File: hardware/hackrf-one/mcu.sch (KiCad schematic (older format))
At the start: 107 parts, among them J1 GSG-USB-MICRO-B, P1 1V8, P17 SSP0, P20 GPIO, P22 I2S, P23 DBGEN, P24 TRST, P25 LPC_ISP, P26 LPC_JTAG, P28 SD, P29 CPLD_JTAG, P3 GND, P30 BANK2_AUX, P8 VCC, SW1 DFU, SW2 RESET, U20 W25Q80BV, U21 TPS62410, U22 GSG-IP4220CZ6, U23 LPC4320FBD144, U24 GSG-XC2C64A-7VQG100C, X2 MCU_XTAL, X3 RTC_XTAL

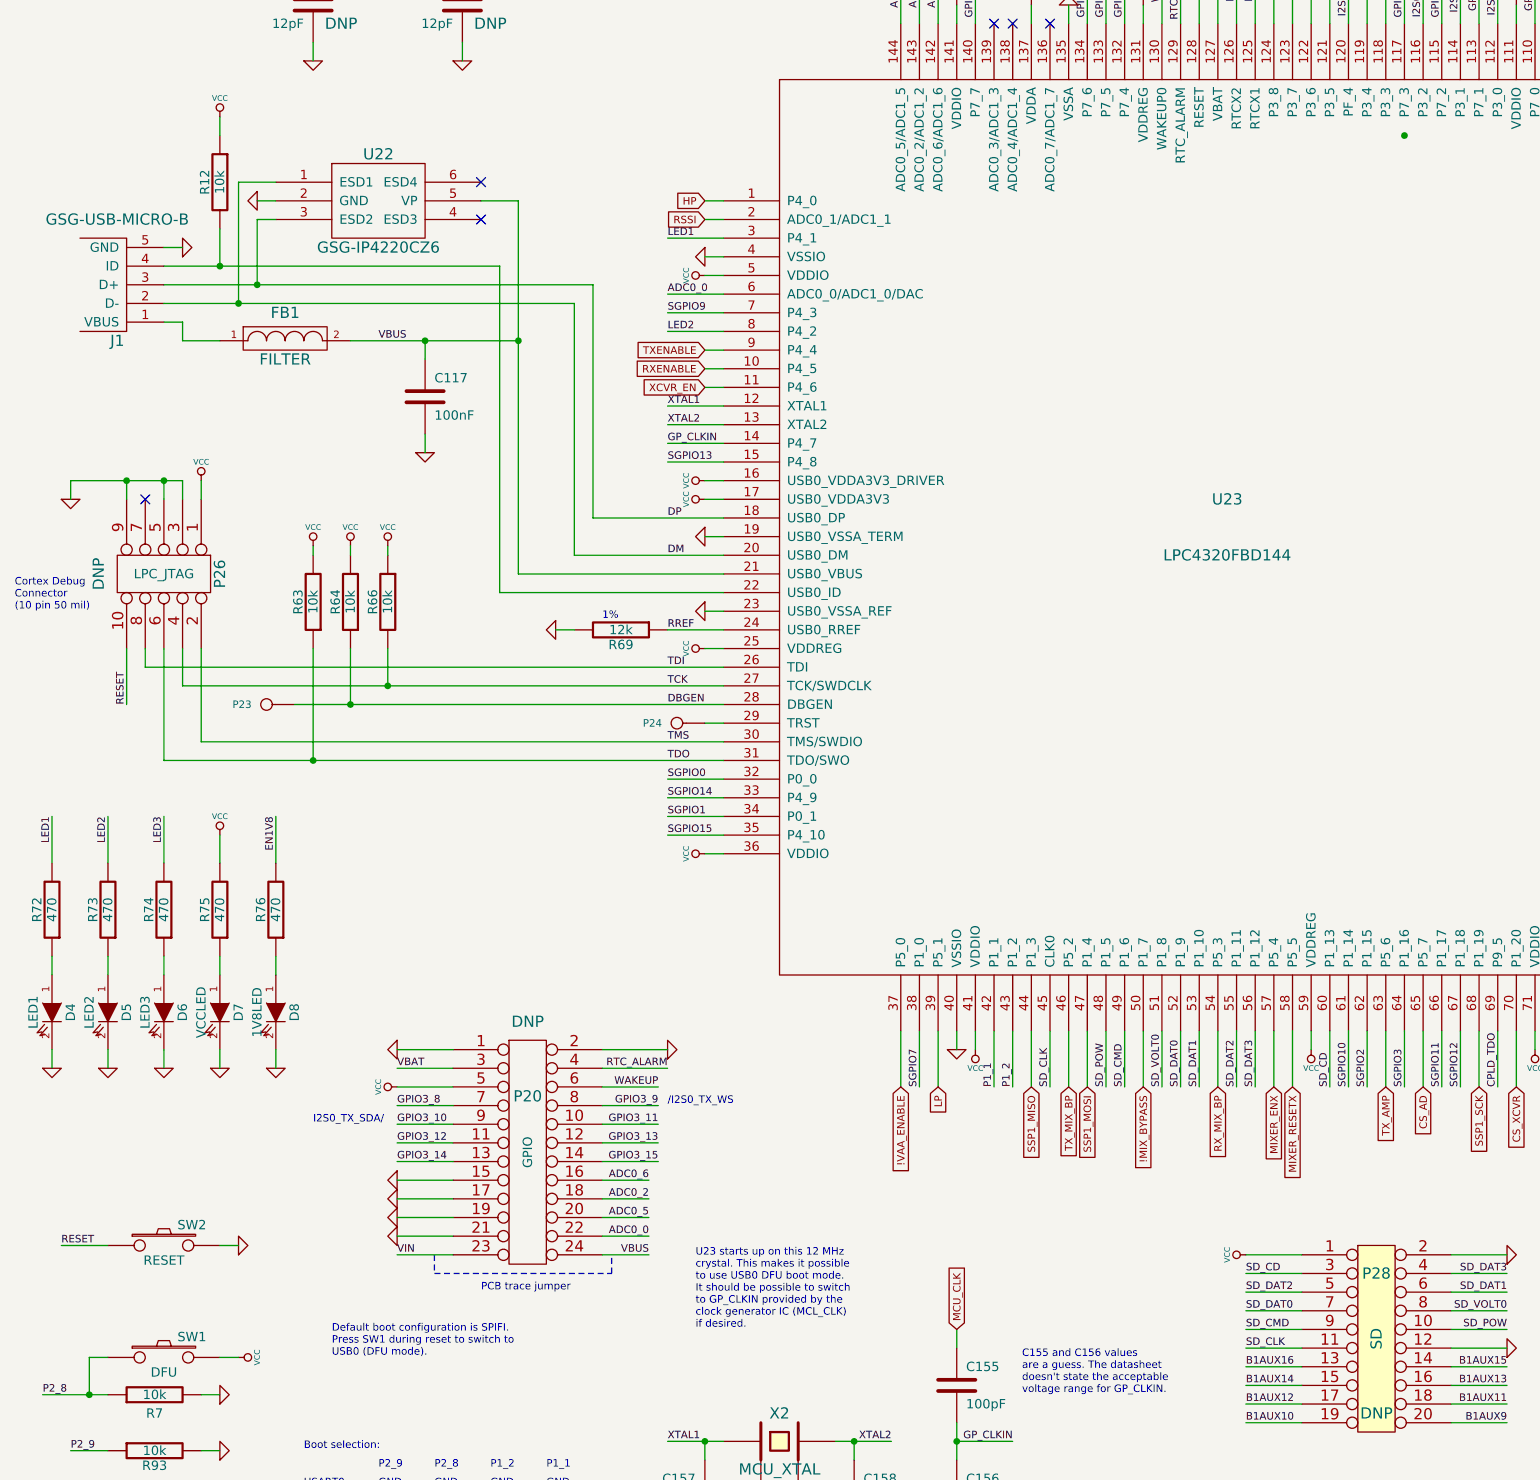
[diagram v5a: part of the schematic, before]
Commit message: pushbutton component selection
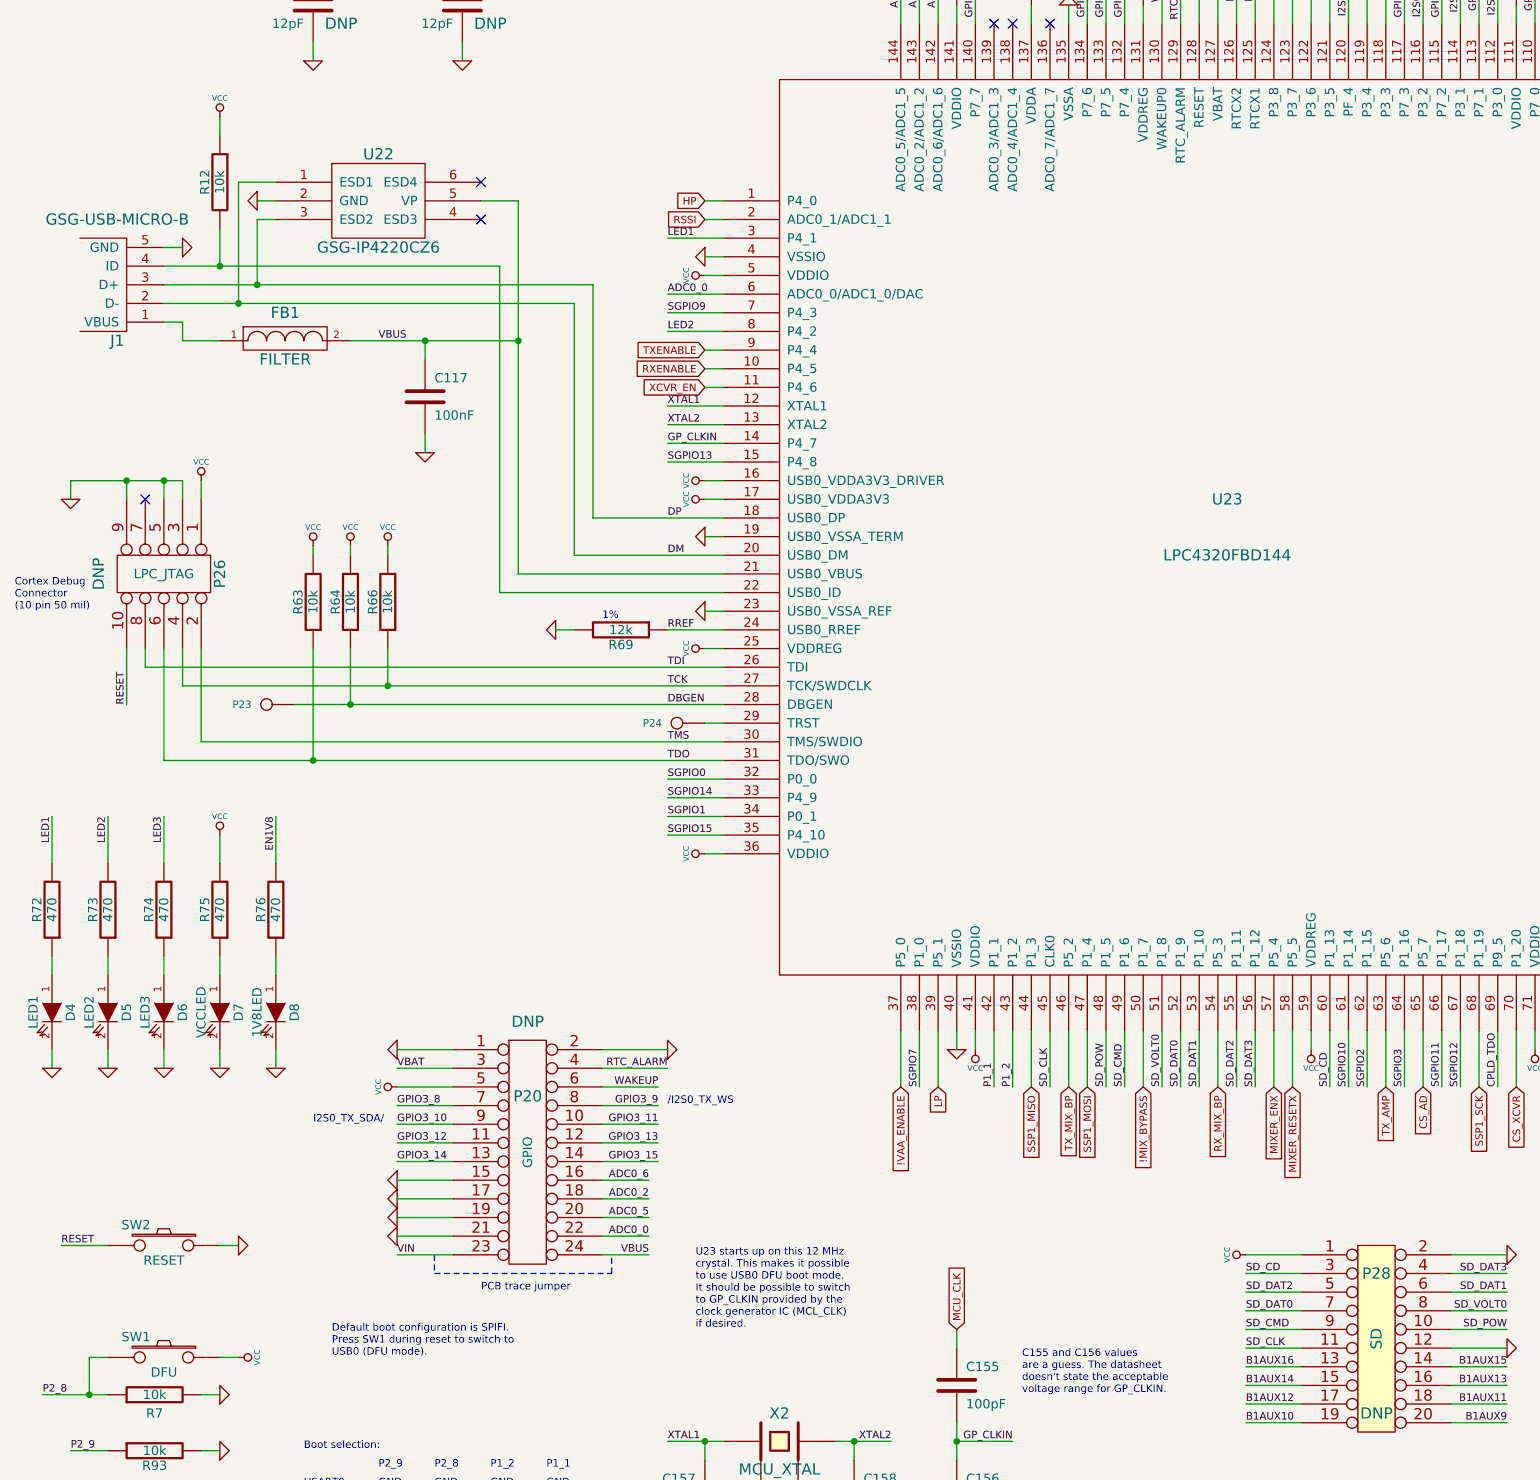
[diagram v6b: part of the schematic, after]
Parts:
- SW1, SW2: Description (none) -> SWITCH PUSH DPDT 0.3A 30V; Manufacturer (none) -> E-Switch; Part Number (none) -> LC2259OANP
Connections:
- net GND: now also SW2.1; no longer SW2.2
- net P2_8: now also SW1.2; no longer SW1.1
- net RESET: now also SW2.2; no longer SW2.1
- net VCC: now also SW1.1; no longer SW1.2
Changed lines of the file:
@@
 Sheet 4 4
 Title "HackRF One mcu/usb/power"
-Date "7 nov 2013"
+Date "9 nov 2013"
 Rev ""
 Comp "Copyright 2012 Michael Ossmann"
@@
 F 2 "" H 1300 9200 60  0000 C CNN
 F 3 "" H 1300 9200 60  0000 C CNN
+F 4 "E-Switch" H 1300 9200 60  0001 C CNN "Manufacturer"
+F 5 "LC2259OANP" H 1300 9200 60  0001 C CNN "Part Number"
+F 6 "SWITCH PUSH DPDT 0.3A 30V" H 1300 9200 60  0001 C CNN "Description"
 	1    1300 9200
-	1    0    0    -1
+	-1   0    0    -1
 $EndComp
 $Comp
@@
 F 2 "" H 1300 8600 60  0000 C CNN
 F 3 "" H 1300 8600 60  0000 C CNN
+F 4 "E-Switch" H 1300 8600 60  0001 C CNN "Manufacturer"
+F 5 "LC2259OANP" H 1300 8600 60  0001 C CNN "Part Number"
+F 6 "SWITCH PUSH DPDT 0.3A 30V" H 1300 8600 60  0001 C CNN "Description"
 	1    1300 8600
-	1    0    0    -1
+	-1   0    0    -1
 $EndComp
 $Comp
@@
 Wire Wire Line
 	11100 7450 10800 7450
-Connection ~ 7950 2650
 Wire Wire Line
 	5850 1200 5950 1200

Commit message: right angle LEDs
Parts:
- D4, D7: Description LED GREEN STD BRIGHT 0603 SMD -> LED GREEN CLEAR RT ANG 0805; Manufacturer Everlight -> Lite-On; Part Number QTLP601C4TR -> LTST-S220KGKT
- D5, D8: Description LED YLW SUPER BRIGHT 0606 SMD -> LED YELLOW CLEAR RT ANG 0805; Manufacturer Everlight -> Lite-On; Part Number QTLP600CYTR -> LTST-S220KSKT
- D6: Description LED RED STD BRIGHT 0603 SMD -> LED SUPR RED CLR RT ANG 0805; Manufacturer Everlight -> Lite-On; Part Number QTLP601CRTR -> LTST-S220KRKT
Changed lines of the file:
@@
 F 2 "" H 1000 7350 60  0001 C CNN
 F 3 "" H 1000 7350 60  0001 C CNN
-F 4 "Everlight" H 1000 7350 60  0001 C CNN "Manufacturer"
-F 5 "QTLP600CYTR" H 1000 7350 60  0001 C CNN "Part Number"
-F 6 "LED YLW SUPER BRIGHT 0606 SMD" H 1000 7350 60  0001 C CNN "Description"
+F 4 "Lite-On" H 1000 7350 60  0001 C CNN "Manufacturer"
+F 5 "LTST-S220KSKT" H 1000 7350 60  0001 C CNN "Part Number"
+F 6 "LED YELLOW CLEAR RT ANG 0805" H 1000 7350 60  0001 C CNN "Description"
 	1    1000 7350
 	0    1    1    0
@@
 F 2 "" H 1900 7350 60  0001 C CNN
 F 3 "" H 1900 7350 60  0001 C CNN
-F 4 "Everlight" H 1900 7350 60  0001 C CNN "Manufacturer"
-F 5 "QTLP600CYTR" H 1900 7350 60  0001 C CNN "Part Number"
-F 6 "LED YLW SUPER BRIGHT 0606 SMD" H 1900 7350 60  0001 C CNN "Description"
+F 4 "Lite-On" H 1900 7350 60  0001 C CNN "Manufacturer"
+F 5 "LTST-S220KSKT" H 1900 7350 60  0001 C CNN "Part Number"
+F 6 "LED YELLOW CLEAR RT ANG 0805" H 1900 7350 60  0001 C CNN "Description"
 	1    1900 7350
 	0    1    1    0
@@
 F 2 "" H 700 7350 60  0001 C CNN
 F 3 "" H 700 7350 60  0001 C CNN
-F 4 "Everlight" H 700 7350 60  0001 C CNN "Manufacturer"
-F 5 "QTLP601C4TR" H 700 7350 60  0001 C CNN "Part Number"
-F 6 "LED GREEN STD BRIGHT 0603 SMD" H 700 7350 60  0001 C CNN "Description"
+F 4 "Lite-On" H 700 7350 60  0001 C CNN "Manufacturer"
+F 5 "LTST-S220KGKT" H 700 7350 60  0001 C CNN "Part Number"
+F 6 "LED GREEN CLEAR RT ANG 0805" H 700 7350 60  0001 C CNN "Description"
 	1    700  7350
 	0    1    1    0
@@
 F 2 "" H 1600 7350 60  0001 C CNN
 F 3 "" H 1600 7350 60  0001 C CNN
-F 4 "Everlight" H 1600 7350 60  0001 C CNN "Manufacturer"
-F 5 "QTLP601C4TR" H 1600 7350 60  0001 C CNN "Part Number"
-F 6 "LED GREEN STD BRIGHT 0603 SMD" H 1600 7350 60  0001 C CNN "Description"
+F 4 "Lite-On" H 1600 7350 60  0001 C CNN "Manufacturer"
+F 5 "LTST-S220KGKT" H 1600 7350 60  0001 C CNN "Part Number"
+F 6 "LED GREEN CLEAR RT ANG 0805" H 1600 7350 60  0001 C CNN "Description"
 	1    1600 7350
 	0    1    1    0
@@
 F 2 "" H 1300 7350 60  0001 C CNN
 F 3 "" H 1300 7350 60  0001 C CNN
-F 4 "Everlight" H 1300 7350 60  0001 C CNN "Manufacturer"
-F 5 "QTLP601CRTR" H 1300 7350 60  0001 C CNN "Part Number"
-F 6 "LED RED STD BRIGHT 0603 SMD" H 1300 7350 60  0001 C CNN "Description"
+F 4 "Lite-On" H 1300 7350 60  0001 C CNN "Manufacturer"
+F 5 "LTST-S220KRKT" H 1300 7350 60  0001 C CNN "Part Number"
+F 6 "LED SUPR RED CLR RT ANG 0805" H 1300 7350 60  0001 C CNN "Description"
 	1    1300 7350
 	0    1    1    0

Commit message: VAA (RF supply) LED
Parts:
- added D?: VAALED, symbol LED
- added R?: 470, symbol R
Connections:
- net GND: now also D?.2 (K)
- new net: D?.1 (A), R?.1
- new net VAA: R?.2
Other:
- moved on the sheet: P20
